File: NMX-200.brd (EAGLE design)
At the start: 67.3 x 63.5 mm, 93 parts, among them IC1 AT90USB1287-AU, IC2 AT90USB1287-MU, J1 PJ-002AH, J2 10118193-0001LF, J3 SJ1-2503A, J4 RJHSE-5385-02, J5 SJ1-2503A, J6 SJ1-2503A, Q1 P-CHANNEL_MOSFET, T1 CMPT2369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

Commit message: Replaced 5V regulator with cold-resistant model
The MC78M05CDTG ON-Semiconductor regulator was replaced with the
MC78M05BDTG. The minimum operating temperature of former is 0°C and the
latter is -45°C. There have been issues connecting to the NMX via
Bluetooth when it is very cold, so this change is being made in an
attempt to address that issue.

The CAM files have not changed at all, but their names have been updated
to Rev 3.
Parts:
- U1: value MC78M05CDTG -> MC78M05BDTG
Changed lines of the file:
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@@
 <?xml version="1.0" encoding="utf-8"?>
 <!DOCTYPE eagle SYSTEM "eagle.dtd">
-<eagle version="6.6.0">
+<eagle version="6.5.0">
 <drawing>
 <settings>
@@
 <attribute name="VALUE" x="6.1595" y="17.30375" size="0.8128" layer="28" rot="MR270"/>
 </element>
-<element name="U1" library="QS_Components" package="DPAK-3" value="MC78M05CDTG" x="40.005" y="19.05" smashed="yes">
-<attribute name="MPN" value="MC78M05CDTRKG" x="69.215" y="-6.35" size="1.778" layer="27" display="off"/>
+<element name="U1" library="QS_Components" package="DPAK-3" value="MC78M05BDTG" x="40.005" y="19.05" smashed="yes">
+<attribute name="MPN" value="MC78M05BDTRKG" x="69.215" y="-6.35" size="1.778" layer="27" display="off"/>
 <attribute name="MF" value="ON Semiconductor" x="69.215" y="-6.35" size="1.778" layer="27" display="off"/>
 <attribute name="NAME" x="32.18" y="22.30375" size="0.8128" layer="25" font="vector"/>

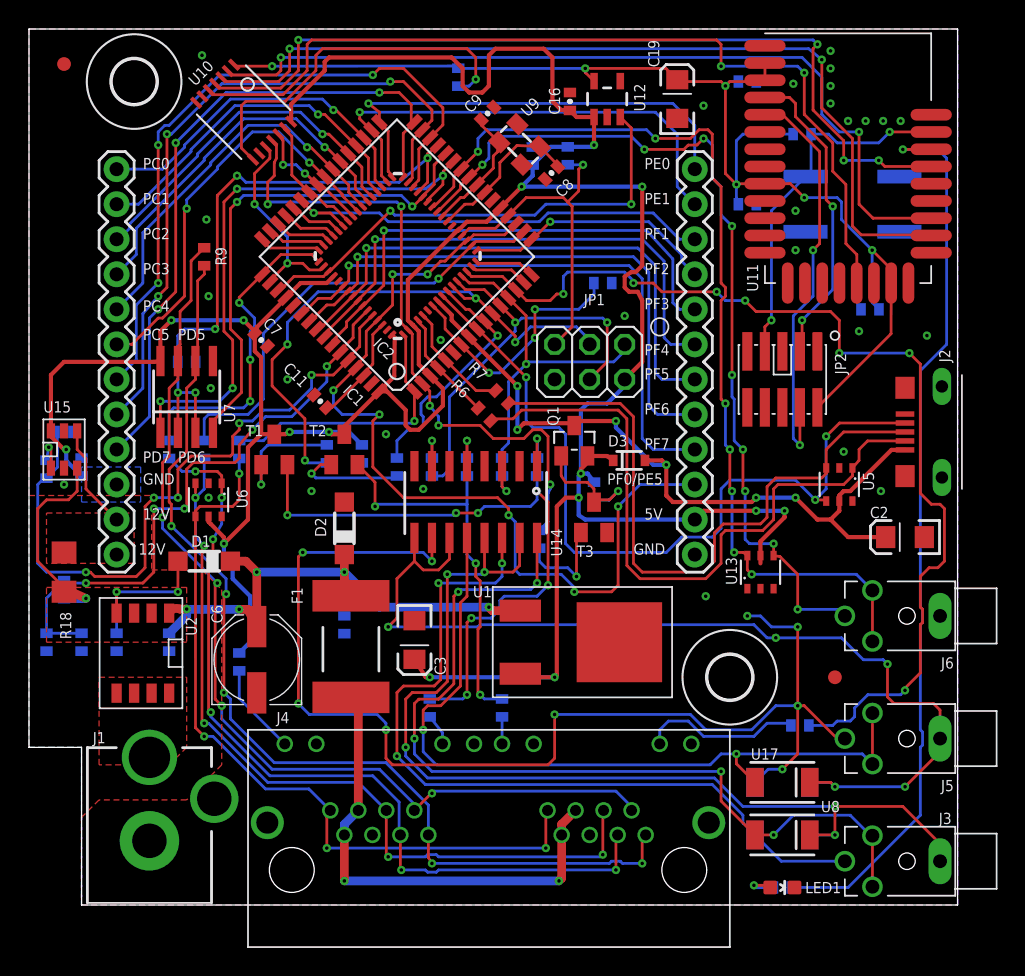
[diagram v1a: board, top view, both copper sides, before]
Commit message: Changed NMX 200 to 4 layer design
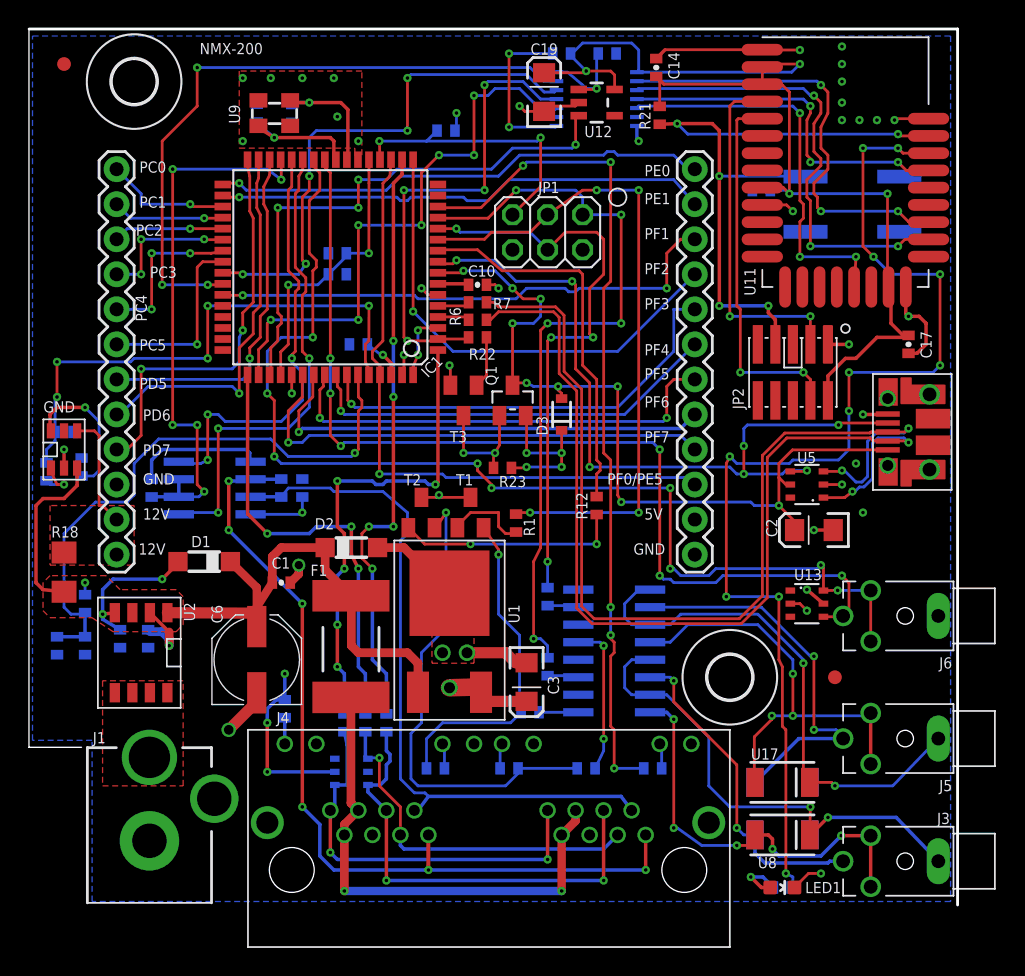
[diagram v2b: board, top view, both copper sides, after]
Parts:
- removed IC2: AT90USB1287-MU, at90usb:MLF64
- removed J2: 10118193-0001LF, PP_Connectors:10118193-0001LF
- added U$5: USB_CONN, dynamic_perception:10118194-0001LF
- R19: value 100 -> 14k
- moved U$1 40.8 mm to (62.7, 26.7)
- moved U10 25.6 mm to (41.1, 58.4), flipped to the bottom, turned to 0 degrees
- moved FB1 24.4 mm to (24.4, 13.2)
- moved FB2 23.8 mm to (25.9, 13.2)
- moved R14 23.5 mm to (40.4, 9.91), turned to 180 degrees
- moved U6 22.3 mm to (23.4, 9.65), flipped to the bottom, turned to 0 degrees
- moved FB3 21.2 mm to (22.9, 13.2)
- moved FRAME2 21.1 mm to (16.9, 62.5), flipped to the top, turned to 180 degrees
- moved C8 19.3 mm to (19.1, 57.4), flipped to the bottom, turned to 270 degrees
- moved U9 17.9 mm to (17.8, 57.4), turned to 270 degrees
- moved R2 17.8 mm to (36.3, 14.0), turned to 180 degrees
- moved R9 17.7 mm to (18.3, 30.2), flipped to the bottom, turned to 90 degrees
- moved C9 16.7 mm to (16.5, 57.4), flipped to the bottom, turned to 90 degrees
- moved C13 15.8 mm to (22.4, 47.2), turned to 0 degrees
- moved R22 15.3 mm to (32.5, 41.1), flipped to the top, turned to 0 degrees
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- renumbered U15 to GND
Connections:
- removed net D+: J2.3, R7.1, U5.3
- removed net D-: J2.2, R6.1, U5.1
- removed net USB+: IC1.5, IC2.5, R7.2
- removed net USB-: IC1.4, IC2.4, R6.2
- new net D_N: R6.1, U$5.P$2, U5.1
- new net D_P: R7.1, U$5.P$3, U5.3
- new net USB_N: IC1.4, R6.2
- new net USB_P: IC1.5, R7.2
- net 3.3V_EN: no longer IC2.51
- net 5V: no longer IC2.21, IC2.3, IC2.52, IC2.64
- net 5V_USB: now also U$5.P$1; no longer IC2.8, J2.1
- net AREF: no longer IC2.62
- net COM1: no longer IC2.49
- net COM2: no longer IC2.18
- net COM3: no longer IC2.1
- net DE: no longer IC2.29
- net E-STOP: no longer IC2.19, IC2.61
- net FOC: no longer IC2.13
- net FOC2: no longer IC2.12
- net GND: now also U$5.P$5; no longer IC2.22, IC2.53, IC2.6, IC2.63, J2.5, J2.S1, J2.S2, J2.S3, J2.S4
- net P1_0_5V: no longer IC2.50
- net PA3: no longer IC2.48
- net PA4: no longer IC2.47
- net PA5: no longer IC2.46
- net PA6: no longer IC2.45
- net PA7: no longer IC2.44
- net PB4: no longer IC2.14
- net PB5: no longer IC2.15
- net PB6: no longer IC2.16
- net PB7: no longer IC2.17
- net PC0: no longer IC2.35
- net PC1: no longer IC2.36
- net PC2: no longer IC2.37
- net PC3: no longer IC2.38
- net PC4: no longer IC2.39
- net PC5: no longer IC2.40
- net PD0: no longer IC2.25
- net PD1: no longer IC2.26
- net PD5: no longer IC2.30
- net PD6: no longer IC2.31
- net PD7: no longer IC2.32
- net PE0: no longer IC2.33
- net PE1: no longer IC2.34
- net PE2: no longer IC2.43
- net PE3: now also U$5.P$4; no longer IC2.9, J2.4
- net PE7: no longer IC2.2
- net PF1: no longer IC2.60
- net PF2: no longer IC2.59
- net PF3: no longer IC2.58
- net PF4: no longer IC2.57
- net PF5: no longer IC2.56
- net PF6: no longer IC2.55
- net PF7: no longer IC2.54
- net RST: no longer IC2.20
- net RXA: no longer IC2.27
- net RX_5V: no longer IC2.41
- net SHT: no longer IC2.11
- net SHT2: no longer IC2.10
- net TXA: no longer IC2.28
- net TX_5V: no longer IC2.42
- net UCAP: no longer IC2.7
- net XTAL1: no longer IC2.24
- net XTAL2: no longer IC2.23
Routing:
- net 5V: track 240.3 -> 85.2 mm, vias 15 -> 18
- net D_N: track 0.00 -> 73.0 mm, vias 0 -> 2
- net D_P: track 0.00 -> 73.0 mm, vias 0 -> 2
- net GND: track 0.00 -> 72.5 mm, vias 29 -> 38
- net CFO2: track 88.0 -> 28.8 mm, vias 9 -> 2
- net D-: track 49.1 -> 0.00 mm
- net D+: track 47.9 -> 0.00 mm
- net TX_5V: track 9.09 -> 47.7 mm, vias 0 -> 3
- net CCO: track 73.8 -> 35.9 mm, vias 5 -> 2
- net P0_1/INT: track 62.7 -> 25.8 mm, vias 4 -> 3
- net P1_0: track 64.8 -> 29.0 mm, vias 2 -> 3
- net COM1_P: track 61.6 -> 26.1 mm, vias 6 -> 1
- net CFO: track 58.8 -> 24.0 mm, vias 3 -> 2
- net CST: track 64.9 -> 30.5 mm
- net CCO2: track 71.8 -> 38.4 mm, vias 5 -> 2
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- added copper zone on layer 15, net 5V
- added copper zone on layer 15, net GND
- added copper zone on layer 2, net GND
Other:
- outline, holes or cut-outs redrawn

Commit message: Fixed broken route, moved oscilator caps to top layer
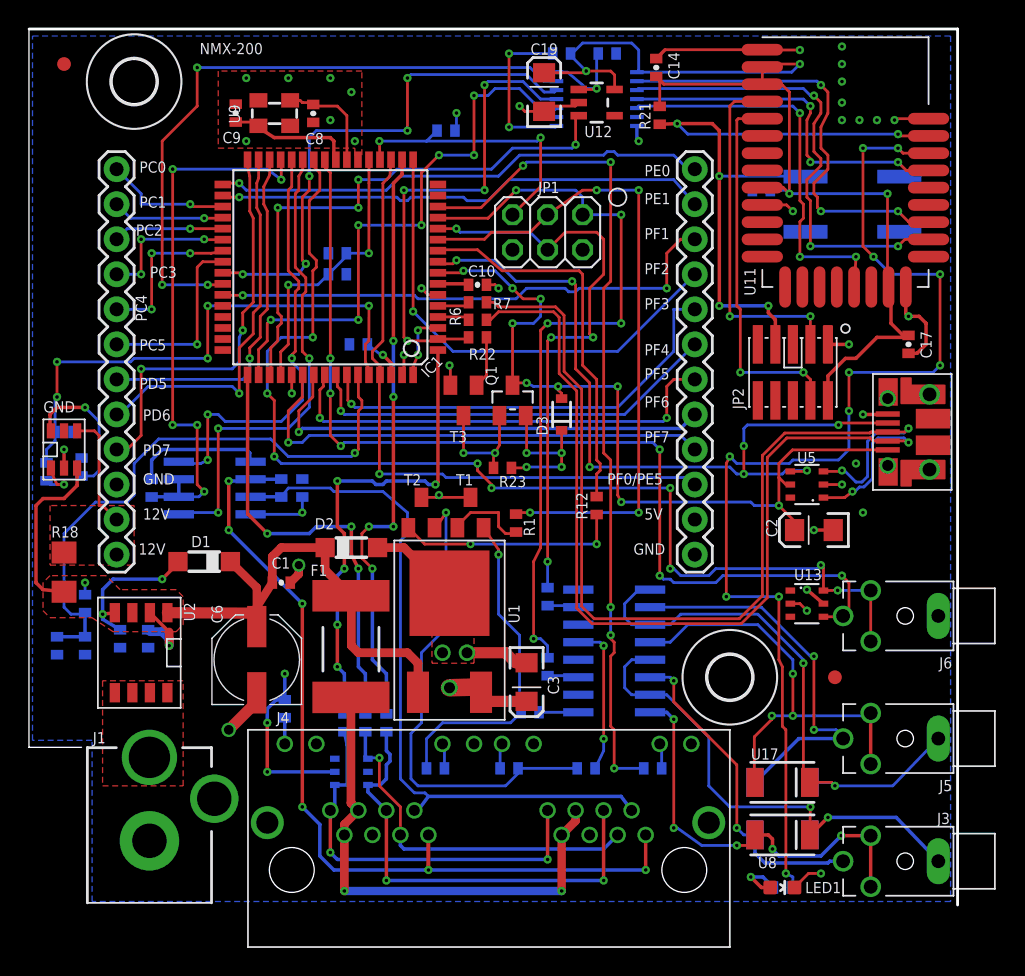
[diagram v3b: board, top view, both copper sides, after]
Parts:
- moved C9 1.52 mm to (15.0, 57.4), flipped to the top
- moved C8 1.52 mm to (20.6, 57.4), flipped to the top
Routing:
- net CCO2: track 38.4 -> 40.3 mm
- net CCO: track 35.9 -> 37.8 mm
- net XTAL2: track 9.42 -> 7.77 mm, vias 1 -> 0
- net XTAL1: track 8.97 -> 9.03 mm, vias 1 -> 0
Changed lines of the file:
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@@
 <attribute name="NAME" x="14.48450625" y="58.021871875" size="0.8128" layer="25" rot="R270"/>
 </element>
-<element name="C8" library="SparkFun-Capacitors" package="0402-CAP" value="12pF" x="19.07949375" y="57.379021875" smashed="yes" rot="MR270">
-<attribute name="MPN" value="C1005C0G1H120J050BA" x="111.789490625" y="11.659025" size="1.778" layer="28" rot="MR270" display="off"/>
-<attribute name="MF" value="TDK Corporation" x="111.789490625" y="11.659025" size="1.778" layer="28" rot="MR270" display="off"/>
-<attribute name="NAME" x="20.603490625" y="57.442521875" size="0.8128" layer="26" rot="MR270"/>
-<attribute name="VALUE" x="19.475234375" y="61.428275" size="0.8128" layer="28" rot="MR270"/>
-</element>
-<element name="C9" library="SparkFun-Capacitors" package="0402-CAP" value="12pF" x="16.51" y="57.404" smashed="yes" rot="MR90">
-<attribute name="MPN" value="C1005C0G1H120J050BA" x="-76.199996875" y="106.933996875" size="1.778" layer="28" rot="MR90" display="off"/>
-<attribute name="MF" value="TDK Corporation" x="-76.199996875" y="106.933996875" size="1.778" layer="28" rot="MR90" display="off"/>
-<attribute name="NAME" x="15.08125" y="56.76899375" size="0.8128" layer="26" rot="MR90"/>
-<attribute name="VALUE" x="16.319503125" y="58.864496875" size="0.8128" layer="28" rot="MR90"/>
+<element name="C8" library="SparkFun-Capacitors" package="0402-CAP" value="12pF" x="20.60349375" y="57.379021875" smashed="yes" rot="R270">
+<attribute name="MPN" value="C1005C0G1H120J050BA" x="-72.106503125" y="11.659025" size="1.778" layer="27" rot="R270" display="off"/>
+<attribute name="MF" value="TDK Corporation" x="-72.106503125" y="11.659025" size="1.778" layer="27" rot="R270" display="off"/>
+<attribute name="NAME" x="20.027478125" y="55.147496875" size="0.8128" layer="25"/>
+<attribute name="VALUE" x="20.105725" y="58.561753125" size="0.8128" layer="27"/>
+</element>
+<element name="C9" library="SparkFun-Capacitors" package="0402-CAP" value="12pF" x="14.986" y="57.404" smashed="yes" rot="R90">
+<attribute name="MPN" value="C1005C0G1H120J050BA" x="107.695996875" y="106.933996875" size="1.778" layer="27" rot="R90" display="off"/>
+<attribute name="MF" value="TDK Corporation" x="107.695996875" y="106.933996875" size="1.778" layer="27" rot="R90" display="off"/>
+<attribute name="NAME" x="15.36700625" y="56.03875" size="0.8128" layer="25" rot="R180"/>
+<attribute name="VALUE" x="15.049503125" y="59.626496875" size="0.8128" layer="27" rot="R180"/>
 </element>
 <element name="C10" library="SparkFun-Capacitors" package="0402-CAP" value=".1uF" x="32.512" y="44.958" smashed="yes" rot="R180">
@@
 <wire x1="19.044" y1="37.09" x2="19.05" y2="37.084" width="0.2032" layer="1"/>
 <polygon width="0.2032" layer="1">
-<vertex x="15.24" y="60.452"/>
-<vertex x="15.24" y="54.864"/>
+<vertex x="13.716" y="60.452"/>
+<vertex x="13.716" y="54.864"/>
 <vertex x="23.622" y="54.864"/>
 <vertex x="23.622" y="54.356"/>
@@
 <vertex x="24.13" y="60.452"/>
 </polygon>
-<via x="17.526" y="59.944" extent="1-16" drill="0.254"/>
+<via x="18.796" y="59.944" extent="1-16" drill="0.254"/>
 <wire x1="36.068" y1="17.56075" x2="35.27125" y2="17.56075" width="0.8128" layer="1"/>
 <wire x1="35.27125" y1="17.56075" x2="34.544" y2="18.288" width="0.8128" layer="1"/>
@@
 <via x="60.198" y="56.896" extent="1-16" drill="0.254" diameter="0.0254"/>
 <via x="61.468" y="56.896" extent="1-16" drill="0.254" diameter="0.0254"/>
-<via x="15.494" y="55.372" extent="1-16" drill="0.254" diameter="0.0254"/>
-<via x="15.494" y="59.944" extent="1-16" drill="0.254" diameter="0.0254"/>
-<via x="19.812" y="59.944" extent="1-16" drill="0.254" diameter="0.0254"/>
-<via x="22.098" y="59.944" extent="1-16" drill="0.254" diameter="0.0254"/>
-<via x="22.352" y="57.15" extent="1-16" drill="0.254" diameter="0.0254"/>
-<via x="23.876" y="55.372" extent="1-16" drill="0.254" diameter="0.0254"/>
+<via x="15.748" y="55.372" extent="1-16" drill="0.254" diameter="0.0254"/>
+<via x="15.748" y="59.944" extent="1-16" drill="0.254" diameter="0.0254"/>
+<via x="21.844" y="59.944" extent="1-16" drill="0.254" diameter="0.0254"/>
+<via x="23.368" y="58.928" extent="1-16" drill="0.254" diameter="0.0254"/>
+<via x="21.844" y="56.896" extent="1-16" drill="0.254" diameter="0.0254"/>
+<via x="23.622" y="55.372" extent="1-16" drill="0.254" diameter="0.0254"/>
 <via x="35.56" y="57.912" extent="1-16" drill="0.254" diameter="0.0254"/>
 <wire x1="35.56" y1="57.912" x2="35.944" y2="57.528" width="0.2032" layer="1"/>
@@
 <wire x1="46.228" y1="15.24" x2="45.018" y2="15.24" width="0.2032" layer="16"/>
 <wire x1="56.595" y1="5.08" x2="56.642" y2="7.112" width="0.2032" layer="1"/>
-<wire x1="56.595" y1="5.08" x2="56.595" y2="5.08" width="0" layer="19" extent="1-16"/>
+<wire x1="56.595" y1="5.08" x2="56.642" y2="5.08" width="0.2032" layer="16"/>
+<wire x1="56.642" y1="5.08" x2="57.912" y2="6.35" width="0.2032" layer="16"/>
 </signal>
 <signal name="CST">
@@
 <wire x1="16.63" y1="56.479" x2="16.975" y2="56.134" width="0.254" layer="1"/>
 <wire x1="16.975" y1="56.134" x2="17.78" y2="55.626" width="0.254" layer="1"/>
-<via x="17.78" y="55.626" extent="1-16" drill="0.254" diameter="0.0254"/>
-<wire x1="16.51" y1="56.754" x2="17.13" y2="56.134" width="0.254" layer="16"/>
-<wire x1="17.13" y1="56.134" x2="17.78" y2="55.626" width="0.254" layer="16"/>
 <wire x1="22.244" y1="54.028" x2="22.098" y2="54.174" width="0.254" layer="1"/>
 <wire x1="22.098" y1="54.174" x2="22.098" y2="55.372" width="0.254" layer="1"/>
 <wire x1="22.098" y1="55.372" x2="21.844" y2="55.626" width="0.254" layer="1"/>
 <wire x1="21.844" y1="55.626" x2="17.78" y2="55.626" width="0.254" layer="1"/>
+<wire x1="14.986" y1="56.754" x2="16.355" y2="56.754" width="0.2032" layer="1"/>
+<wire x1="16.355" y1="56.754" x2="16.63" y2="56.479" width="0.2032" layer="1"/>
 </signal>
 <signal name="XTAL2">
@@
 <contactref element="U9" pad="1"/>
 <contactref element="C8" pad="1"/>
-<wire x1="18.93" y1="58.329" x2="19.093" y2="58.166" width="0.254" layer="1"/>
-<wire x1="19.093" y1="58.166" x2="20.32" y2="58.166" width="0.254" layer="1"/>
-<via x="20.32" y="58.166" extent="1-16" drill="0.254" diameter="0.0254"/>
-<wire x1="19.07949375" y1="58.029021875" x2="19.216471875" y2="58.166" width="0.254" layer="16"/>
-<wire x1="19.216471875" y1="58.166" x2="20.32" y2="58.166" width="0.254" layer="16"/>
-<wire x1="23.044" y1="54.028" x2="23.114" y2="54.098" width="0.254" layer="1"/>
-<wire x1="23.114" y1="54.098" x2="23.114" y2="57.658" width="0.254" layer="1"/>
-<wire x1="23.114" y1="57.658" x2="22.606" y2="58.166" width="0.254" layer="1"/>
-<wire x1="22.606" y1="58.166" x2="20.32" y2="58.166" width="0.254" layer="1"/>
+<wire x1="18.93" y1="58.329" x2="19.649" y2="58.329" width="0.2032" layer="1"/>
+<wire x1="19.649" y1="58.329" x2="19.812" y2="58.166" width="0.2032" layer="1"/>
+<wire x1="19.812" y1="58.166" x2="20.466515625" y2="58.166" width="0.2032" layer="1"/>
+<wire x1="20.466515625" y1="58.166" x2="20.60349375" y2="58.029021875" width="0.2032" layer="1"/>
+<wire x1="23.044" y1="54.028" x2="23.044" y2="57.22" width="0.2032" layer="1"/>
+<wire x1="23.044" y1="57.22" x2="22.352" y2="57.912" width="0.2032" layer="1"/>
+<wire x1="22.352" y1="57.912" x2="20.720515625" y2="57.912" width="0.2032" layer="1"/>
+<wire x1="20.720515625" y1="57.912" x2="20.60349375" y2="58.029021875" width="0.2032" layer="1"/>
 </signal>
 <signal name="USB_P">
@@
 <wire x1="58.42" y1="8.636" x2="58.166" y2="8.89" width="0.2032" layer="1"/>
 <wire x1="58.166" y1="8.89" x2="56.595" y2="8.89" width="0.2032" layer="1"/>
-<wire x1="56.595" y1="8.89" x2="56.595" y2="8.89" width="0" layer="19" extent="1-16"/>
+<wire x1="56.595" y1="8.89" x2="58.166" y2="8.89" width="0.2032" layer="16"/>
+<wire x1="58.166" y1="8.89" x2="58.42" y2="8.636" width="0.2032" layer="16"/>
 </signal>
 <signal name="PD0">

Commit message: Fixed DRC errors
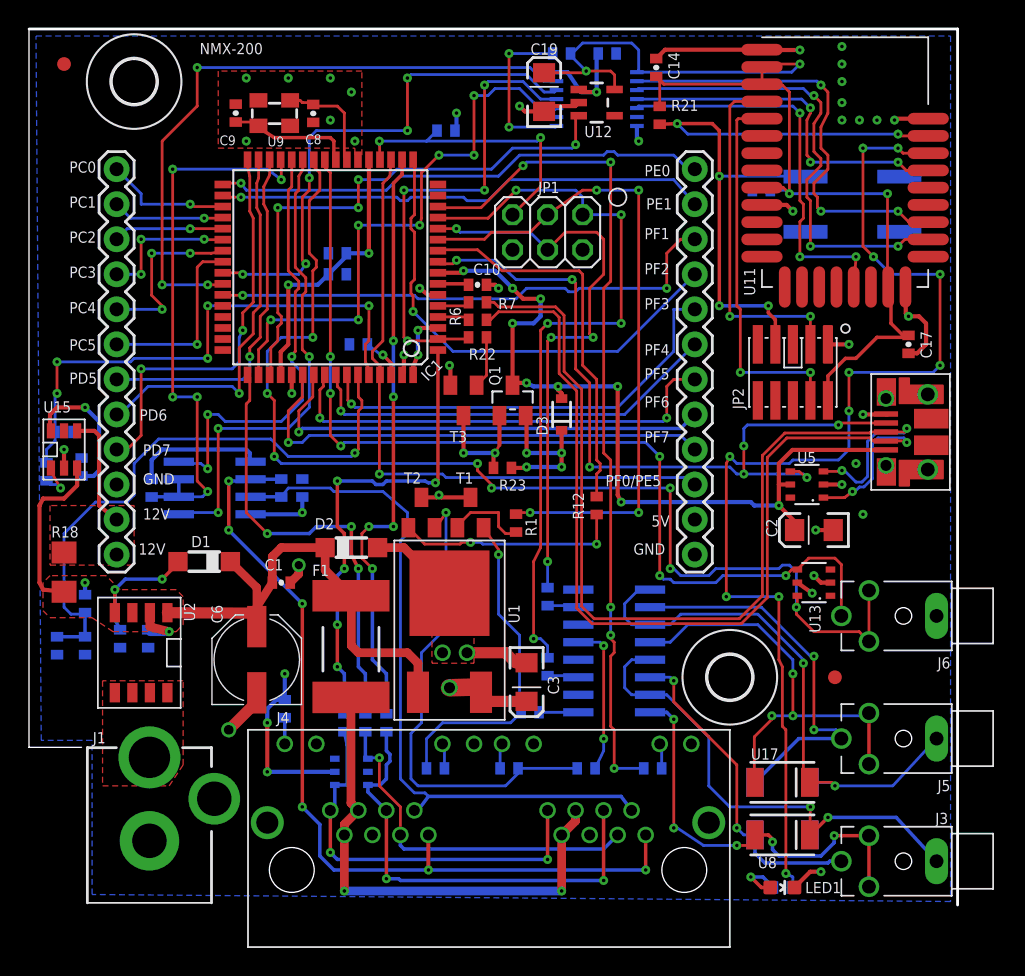
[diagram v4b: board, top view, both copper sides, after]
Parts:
- moved U13 1.61 mm to (56.9, 23.4), turned to 180 degrees
- moved U$2 1.14 mm to (17.0, 48.5)
- moved U$5 0.13 mm to (65.2, 34.3)
- moved J3 0.13 mm to (63.2, 3.17)
- moved J5 0.13 mm to (63.2, 12.1)
- moved J6 0.13 mm to (63.2, 21.0)
- renumbered GND to U15
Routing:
- net PD1: track 81.7 -> 84.7 mm, vias 9 -> 8
- net 12V: track 54.4 -> 52.9 mm
- net PC4: track 12.3 -> 13.4 mm
- net 3.3V: track 81.4 -> 82.2 mm
- net N$5: track 10.9 -> 10.2 mm
- net TXA: track 31.6 -> 32.3 mm
- net PD0: track 72.2 -> 71.5 mm
